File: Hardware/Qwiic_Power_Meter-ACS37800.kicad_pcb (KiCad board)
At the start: 2 copper layers, 30.5 x 38.1 mm, 54 parts, among them J1 Conn_01x01, J10 Conn_01x01, J11 Conn_01x01, J12 I2C, J3 Qwiic_RA, J4 Conn_01x01, J5 Conn_01x01, J6 Conn_01x01, J7 Qwiic_RA, J8 Conn_01x01, J9 Conn_01x01, U1 ACS37800

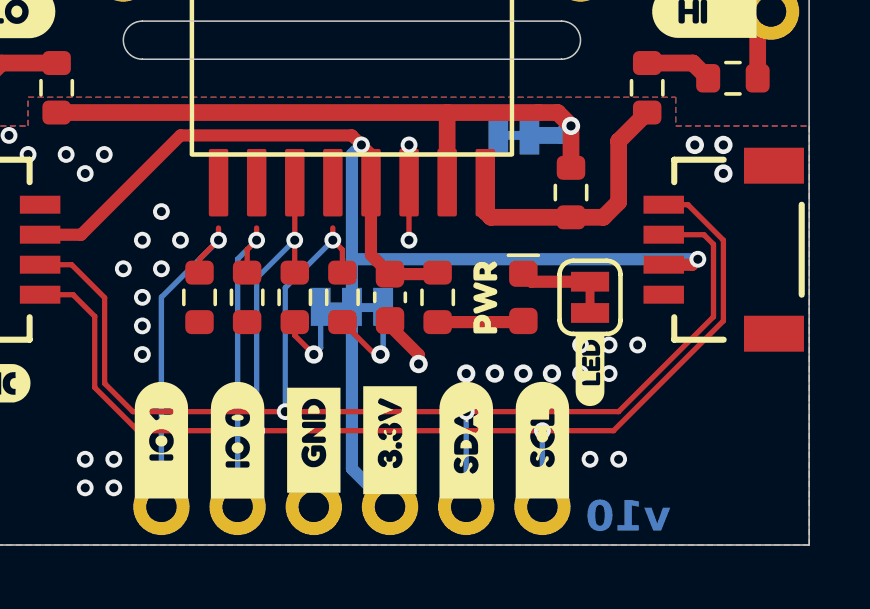
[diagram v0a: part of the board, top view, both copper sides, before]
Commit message: Fixes some missing traces
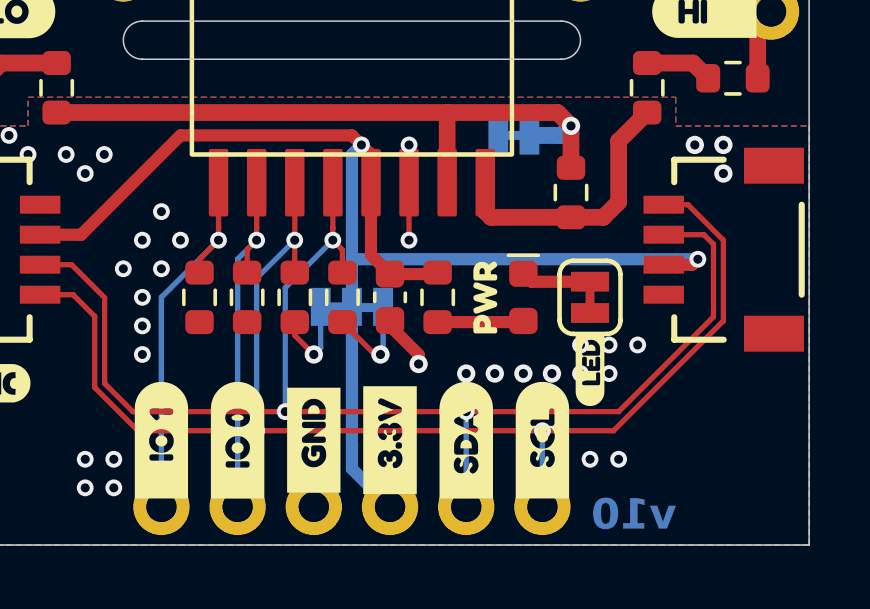
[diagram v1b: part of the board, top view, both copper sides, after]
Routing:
- net IO0: track 10.8 -> 12.3 mm
- net SDA: track 42.8 -> 44.3 mm
- net IO1: track 11.4 -> 12.9 mm
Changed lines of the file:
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@@
 			(psa4output no)
 			(plot_black_and_white yes)
-			(plotinvisibletext no)
 			(sketchpadsonfab no)
 			(plotpadnumbers no)
@@
 				(font
 					(size 0.001 0.001)
+					(thickness 0.15)
 				)
 			)
@@
 				(font
 					(size 0.001 0.001)
+					(thickness 0.15)
 				)
 			)
@@
 	)
 	(gr_text "v10"
-		(at 147.32 114.935 0)
+		(at 147.5105 114.8715 0)
 		(layer "B.Cu" knockout)
 		(effects
@@
 		(net 5)
 	)
+	(segment
+		(start 133.665501 105.3205)
+		(end 133.6675 105.318501)
+		(width 0.1778)
+		(layer "F.Cu")
+		(net 5)
+	)
+	(segment
+		(start 133.6675 105.318501)
+		(end 133.6675 103.81)
+		(width 0.1778)
+		(layer "F.Cu")
+		(net 5)
+	)
 	(via
 		(at 133.665501 105.7275)
@@
 	)
 	(segment
+		(start 137.4775 105.3185)
+		(end 137.4775 103.81)
+		(width 0.1778)
+		(layer "F.Cu")
+		(net 6)
+	)
+	(segment
 		(start 137.795 106.047)
 		(end 137.4755 105.7275)
@@
 	)
 	(segment
+		(start 137.4755 105.3205)
+		(end 137.4775 105.3185)
+		(width 0.1778)
+		(layer "F.Cu")
+		(net 6)
+	)
+	(segment
 		(start 129.8702 110.5027)
 		(end 130.81 111.4425)
@@
 	)
 	(segment
+		(start 134.9355 105.3205)
+		(end 134.9375 105.3185)
+		(width 0.1778)
+		(layer "F.Cu")
+		(net 12)
+	)
+	(segment
+		(start 134.9375 105.3185)
+		(end 134.9375 103.81)
+		(width 0.1778)
+		(layer "F.Cu")
+		(net 12)
+	)
+	(segment

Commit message: Adds ordering instructions, updates design by, revised by
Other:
- board text added: "Finish: HASL Lead-Free"
- board text added: "Layers: 2"
- board text added: "Material: TG135"
- board text added: "Ordering Notes"
- board text added: "Outer Copper Weight: 1oz"
- board text added: "Silkscreen Color: White"
- board text added: "Solder Mask: Red"
- board text added: "Thickness: 1.6mm"
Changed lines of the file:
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@@
 	)
 	(paper "A4")
+	(title_block
+		(title "SparkFun Power Meter ACS37800")
+		(date "2025-07-11")
+		(rev "v10")
+		(company "SparkFun Electronics")
+		(comment 1 "Design By: Nick Poole")
+		(comment 2 "Revised By: Elias Santistevan")
+	)
 	(layers
 		(0 "F.Cu" signal)
@@
 				(color "#FFFFFFFF")
 			)
-			(copper_finish "None")
+			(copper_finish "HAL lead-free")
 			(dielectric_constraints no)
 		)
@@
 		)
 	)
+	(gr_text "Silkscreen Color: White"
+		(at 222.8725 175.2925 0)
+		(layer "Eco1.User")
+		(effects
+			(font
+				(size 1.27 1.27)
+				(thickness 0.15)
+			)
+			(justify left bottom)
+		)
+	)
+	(gr_text "Thickness: 1.6mm"
+		(at 222.8725 179.1025 0)
+		(layer "Eco1.User")
+		(effects
+			(font
+				(size 1.27 1.27)
+				(thickness 0.15)
+			)
+			(justify left bottom)
+		)
+	)
+	(gr_text "Solder Mask: Red"
+		(at 222.8725 173.3875 0)
+		(layer "Eco1.User")
+		(effects
+			(font
+				(size 1.27 1.27)
+				(thickness 0.15)
+			)
+			(justify left bottom)
+		)
+	)
+	(gr_text "Finish: HASL Lead-Free"
+		(at 222.8725 181.0075 0)
+		(layer "Eco1.User")
+		(effects
+			(font
+				(size 1.27 1.27)
+				(thickness 0.15)
+			)
+			(justify left bottom)
+		)
+	)
+	(gr_text "Ordering Notes"
+		(at 216.5225 170.2125 0)
+		(layer "Eco1.User")
+		(effects
+			(font
+				(size 2 2)
+				(thickness 0.15)
+			)
+			(justify left bottom)
+		)
+	)
+	(gr_text "Outer Copper Weight: 1oz"
+		(at 253.3525 177.515 0)
+		(layer "Eco1.User")
+		(effects
+			(font
+				(size 1.27 1.27)
+				(thickness 0.15)
+			)
+			(justify left bottom)
+		)
+	)
+	(gr_text "Layers: 2"
+		(at 222.823392 177.1975 0)
+		(layer "Eco1.User")
+		(effects
+			(font
+				(size 1.27 1.27)
+				(thickness 0.15)
+			)
+			(justify left bottom)
+		)
+	)
+	(gr_text "Material: TG135"
+		(at 253.3525 175.2925 0)
+		(layer "Eco1.User")
+		(effects
+			(font
+				(size 1.27 1.27)
+				(thickness 0.15)
+			)
+			(justify left bottom)
+		)
+	)
 	(dimension
 		(type orthogonal)
@@
 			(keep_text_aligned yes)
 		)
-		(gr_text "0.5 in"
+		(gr_text "12.7 mm"
 			(at 138.1125 118.23 0)
 			(layer "Dwgs.User")
@@
 			(keep_text_aligned yes)
 		)
-		(gr_text "1.5 in"
+		(gr_text "38.1 mm"
 			(at 111.5625 96.8375 90)
 			(layer "Dwgs.User")
@@
 			(keep_text_aligned yes)
 		)
-		(gr_text "0.7 in"
+		(gr_text "17.78 mm"
 			(at 115.69 106.9975 90)
 			(layer "Dwgs.User")
@@
 			(keep_text_aligned yes)
 		)
-		(gr_text "1.2 in"
+		(gr_text "30.48 mm"
 			(at 138.1125 122.6115 0)
 			(layer "Dwgs.User")
@@
 			(keep_text_aligned yes)
 		)
-		(gr_text "0.35 in"
+		(gr_text "8.89 mm"
 			(at 127.3175 118.23 0)
 			(layer "Dwgs.User")
@@
 			(keep_text_aligned yes)
 		)
-		(gr_text "0.2625 in"
+		(gr_text "6.6675 mm"
 			(at 126.20625 72.8275 0)
 			(layer "Dwgs.User")
@@
 			(keep_text_aligned yes)
 		)
-		(gr_text "0.675 in"
+		(gr_text "17.145 mm"
 			(at 138.1125 72.8275 0)
 			(layer "Dwgs.User")
@@
 			(keep_text_aligned yes)
 		)
-		(gr_text "0.2625 in"
+		(gr_text "6.6675 mm"
 			(at 115.2525 81.5975 90)
 			(layer "Dwgs.User")
@@
 			(keep_text_aligned yes)
 		)
-		(gr_text "0.3875 in"
+		(gr_text "9.8425 mm"
 			(at 119.1825 110.96625 90)
 			(layer "Dwgs.User")

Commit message: Adds some more notes to the design
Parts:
- added G***: Flame, SparkFun-Aesthetic:SparkFun_Flame_5mm, F.Cu at (149.9, 112.4)

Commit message: Fixes silk
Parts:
- removed kibuzzard-67B80A2B (x2): G***, kibuzzard-67B80A2B
- removed kibuzzard-67B80A30 (x2): G***, kibuzzard-67B80A30
- removed kibuzzard-67B80A4B (x2): G***, kibuzzard-67B80A4B
- removed kibuzzard-67B80A82 (x2): G***, kibuzzard-67B80A82
- removed kibuzzard-67B80A93 (x2): G***, kibuzzard-67B80A93
- removed kibuzzard-67B80A9A (x2): G***, kibuzzard-67B80A9A
- removed kibuzzard-67B81068: G***, kibuzzard-67B81068
- removed kibuzzard-67B81094: G***, kibuzzard-67B81094
- removed kibuzzard-67B810A5: G***, kibuzzard-67B810A5
- removed kibuzzard-67B815F9: G***, kibuzzard-67B815F9
- removed kibuzzard-67B8162A: G***, kibuzzard-67B8162A
- removed kibuzzard-67B81692: G***, kibuzzard-67B81692
- removed kibuzzard-67B816A9: G***, kibuzzard-67B816A9
- removed kibuzzard-681260C2: G***, kibuzzard-681260C2
- added kibuzzard-68C98CE2: G***, kibuzzard-68C98CE2, B.Cu at (151.6, 95.9)
- added kibuzzard-68C98CF7: G***, kibuzzard-68C98CF7, F.Cu at (126.5, 98.1)
- added kibuzzard-68C98D0A: G***, kibuzzard-68C98D0A, F.Cu at (150.0, 98.1)
- added kibuzzard-68C98D92: G***, kibuzzard-68C98D92, F.Cu at (131.8, 112.2)
- added kibuzzard-68C98DAC: G***, kibuzzard-68C98DAC, F.Cu at (134.3, 112.0)
- added kibuzzard-68C98DC2: G***, kibuzzard-68C98DC2, F.Cu at (136.9, 112.2)
- added kibuzzard-68C98DD6: G***, kibuzzard-68C98DD6, F.Cu at (139.4, 112.2)
- added kibuzzard-68C98DF7: G***, kibuzzard-68C98DF7, F.Cu at (141.9, 112.0)
- added kibuzzard-68C98E17: G***, kibuzzard-68C98E17, F.Cu at (144.5, 112.1)
- added kibuzzard-68C98F03: G***, kibuzzard-68C98F03, F.Cu at (146.1, 110.0)
- added kibuzzard-68C98FF6: G***, kibuzzard-68C98FF6, B.Cu at (131.8, 112.2)
- added kibuzzard-68C99001: G***, kibuzzard-68C99001, B.Cu at (134.3, 112.0)
- added kibuzzard-68C99018: G***, kibuzzard-68C99018, B.Cu at (144.5, 112.1)
- added kibuzzard-68C9901D: G***, kibuzzard-68C9901D, B.Cu at (141.9, 112.0)
- added kibuzzard-68C99023: G***, kibuzzard-68C99023, B.Cu at (139.4, 112.2)
- added kibuzzard-68C99027: G***, kibuzzard-68C99027, B.Cu at (136.9, 112.2)
- added kibuzzard-68C9907C: G***, kibuzzard-68C9907C, B.Cu at (141.3, 108.0)
- added kibuzzard-68C99085: G***, kibuzzard-68C99085, B.Cu at (146.9, 102.3)
- added kibuzzard-68C99129: G***, kibuzzard-68C99129, B.Cu at (126.5, 98.1)
- added kibuzzard-68C9913E: G***, kibuzzard-68C9913E, B.Cu at (150.0, 98.1)
- moved Ref** 23.6 mm to (125.7, 113.4)

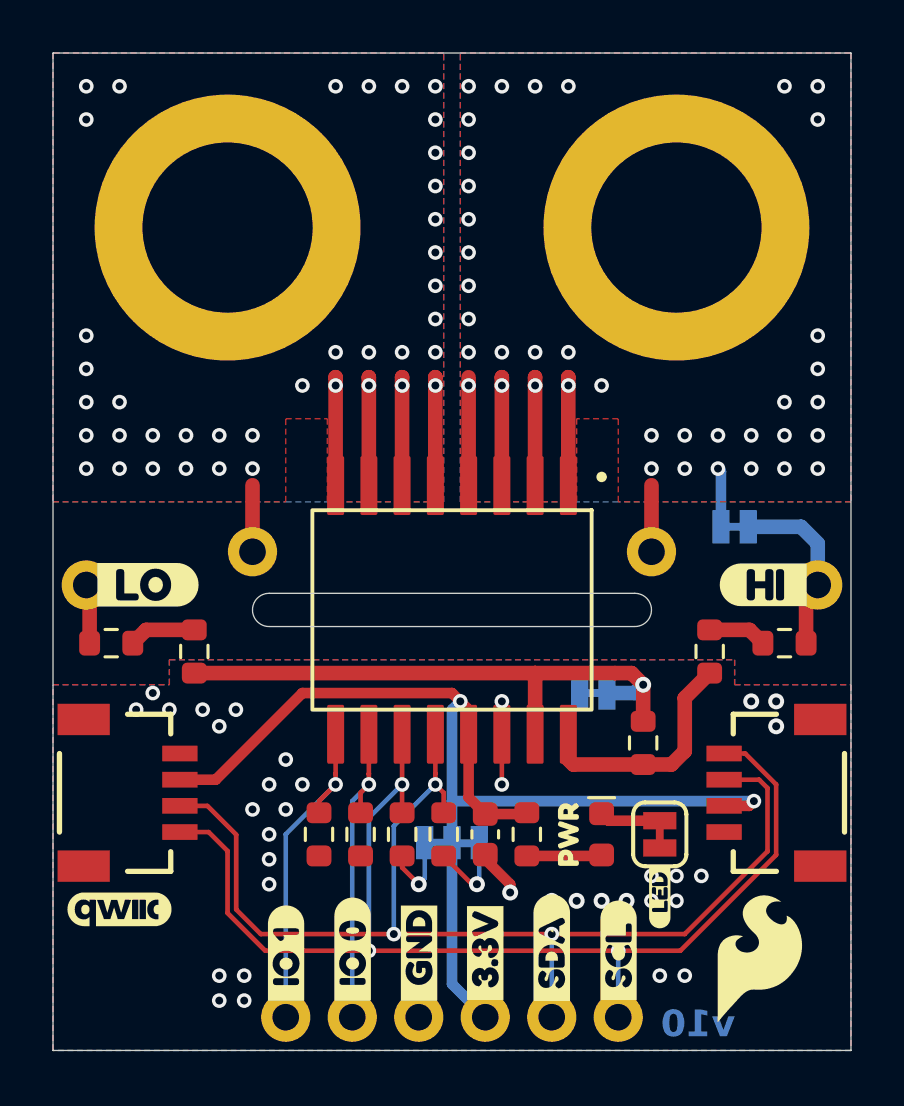
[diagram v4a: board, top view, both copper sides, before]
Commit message: Adds fiducials and standoffs, changes the silk on the underside
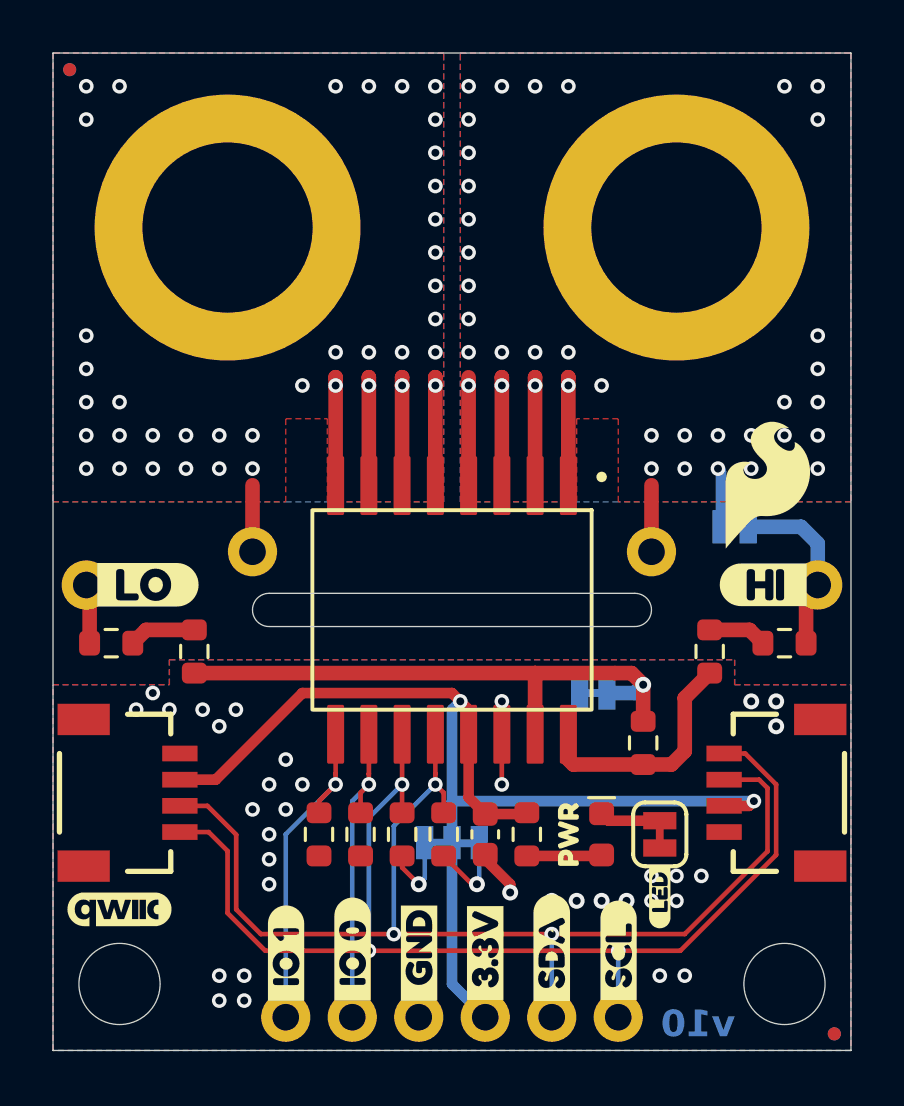
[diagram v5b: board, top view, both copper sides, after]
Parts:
- removed kibuzzard-67B81183: G***, kibuzzard-67B81183
- added FID1: Fiducial_0.5mm, SparkFun-Aesthetic:Fiducial_0.5mm_Mask1mm, F.Cu at (152.7, 115.3)
- added FID2: Fiducial_0.5mm, SparkFun-Aesthetic:Fiducial_0.5mm_Mask1mm, B.Cu at (152.7, 115.3)
- added FID3: Fiducial_0.5mm, SparkFun-Aesthetic:Fiducial_0.5mm_Mask1mm, F.Cu at (123.5, 78.4)
- added FID4: Fiducial_0.5mm, SparkFun-Aesthetic:Fiducial_0.5mm_Mask1mm, B.Cu at (123.5, 78.4)
- added ST1: Standoff, SparkFun-Hardware:Standoff, F.Cu at (125.4, 113.3)
- added ST2: Standoff, SparkFun-Hardware:Standoff, F.Cu at (150.8, 113.3)
- added kibuzzard-68C9961E: G***, kibuzzard-68C9961E, B.Cu at (130.8, 108.0)
- added kibuzzard-68C99652: G***, kibuzzard-68C99652, B.Cu at (130.8, 106.4)
- JP1: value ~ -> LED
- JP2: value ~ -> I2C
- moved G*** 18.1 mm to (150.2, 94.3)
- moved Ref** 3.71 mm to (128.6, 111.1)
- moved G*** 1.59 mm to (130.8, 104.8)
- renumbered JP3 to IP+1, JP4 to VINN1
